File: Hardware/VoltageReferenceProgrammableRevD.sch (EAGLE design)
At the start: 57 parts, among them J1 AVR_SPI_PRG_6PTH, J2 POWER_JACKPTH, U1 MIC5205, U2 REF5040ID, U3 ATMEGA328, U4 SN74LV164APW, U5 AD5040BRJZ, U6 OPA365, Y1 16MHz

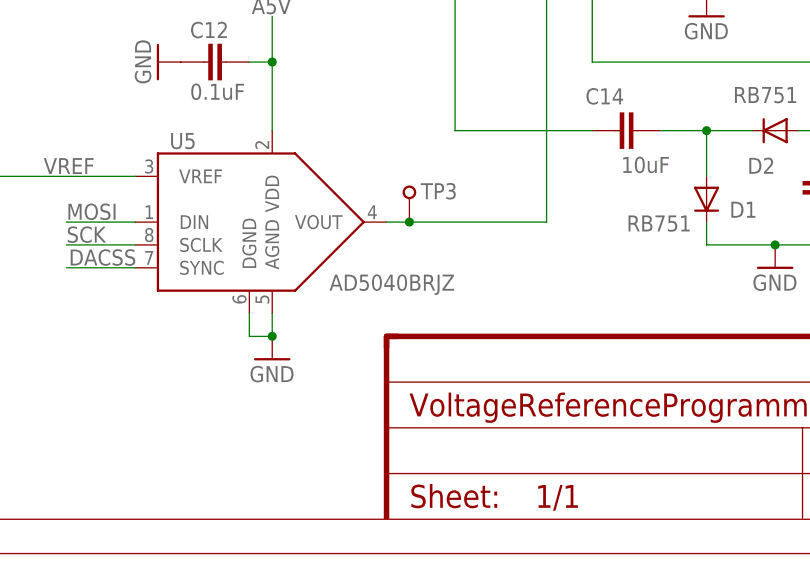
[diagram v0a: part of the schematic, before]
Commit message: Corrected error on schematic & BOM
AD5040 was replaced with AD5060.
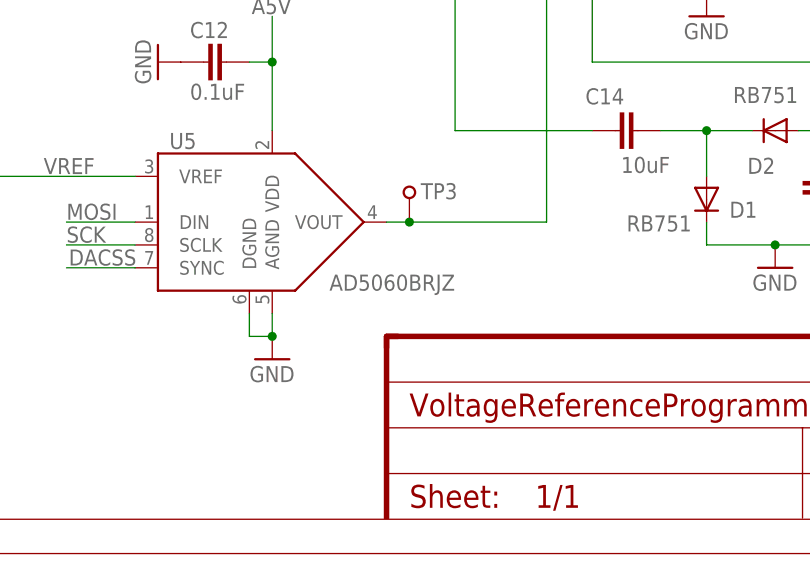
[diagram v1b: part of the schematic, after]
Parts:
- U5: value AD5040BRJZ -> AD5060BRJZ
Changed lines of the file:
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@@
 <part name="C8" library="SparkFun-Capacitors" deviceset="CAP" device="0805" value="10uF"/>
 <part name="Y1" library="SparkFun-FreqCtrl" deviceset="RESONATOR" device="SMD" value="16MHz"/>
-<part name="U5" library="ChipsParts" deviceset="AD5040" device="BRJZ"/>
+<part name="U5" library="ChipsParts" deviceset="AD5040" device="BRJZ" value="AD5060BRJZ"/>
 <part name="J2" library="SparkFun-Connectors" deviceset="POWER_JACK" device="PTH"/>
 <part name="TP1" library="ChipsParts" deviceset="TEST_POINT" device=""/>
